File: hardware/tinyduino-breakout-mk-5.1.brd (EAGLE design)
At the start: 24 x 22 mm, 12 parts, among them J1 DF12-32-DP-NOTREALLYREV

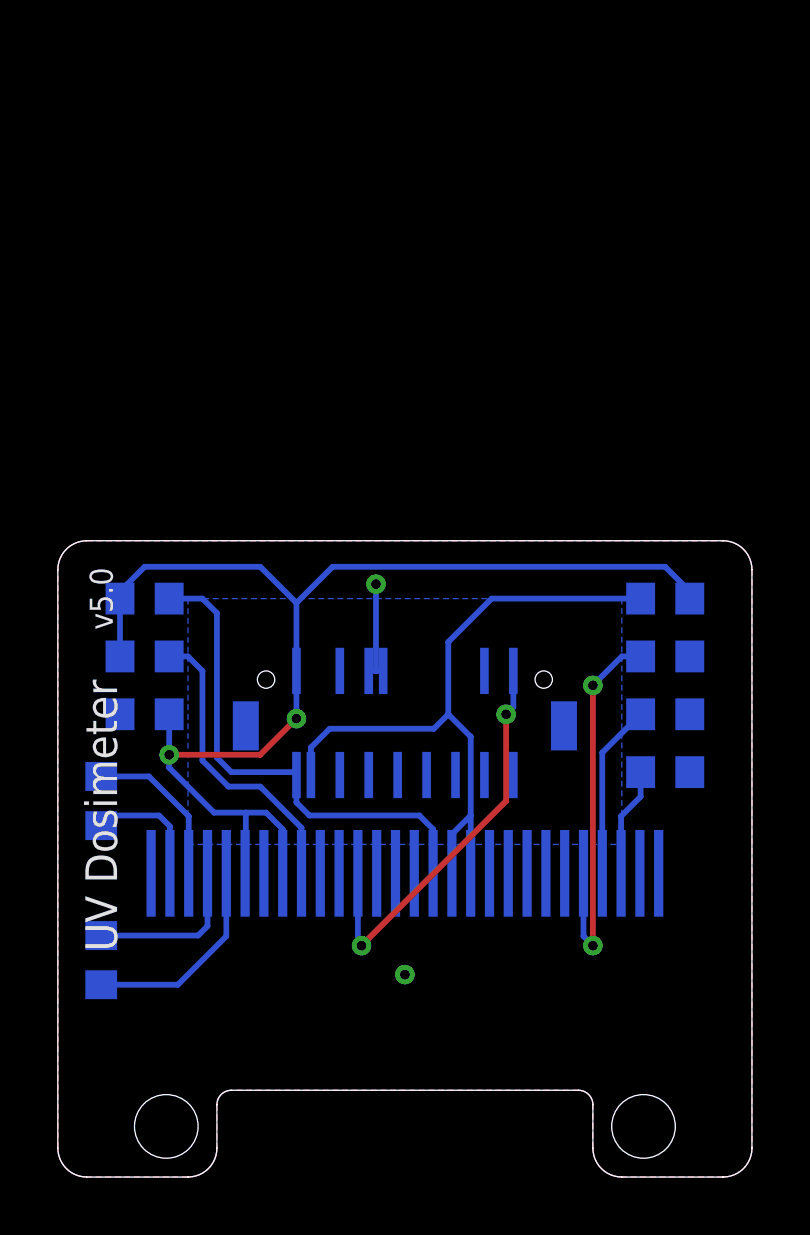
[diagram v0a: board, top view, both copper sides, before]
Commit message: breakouts for the tinyduino version
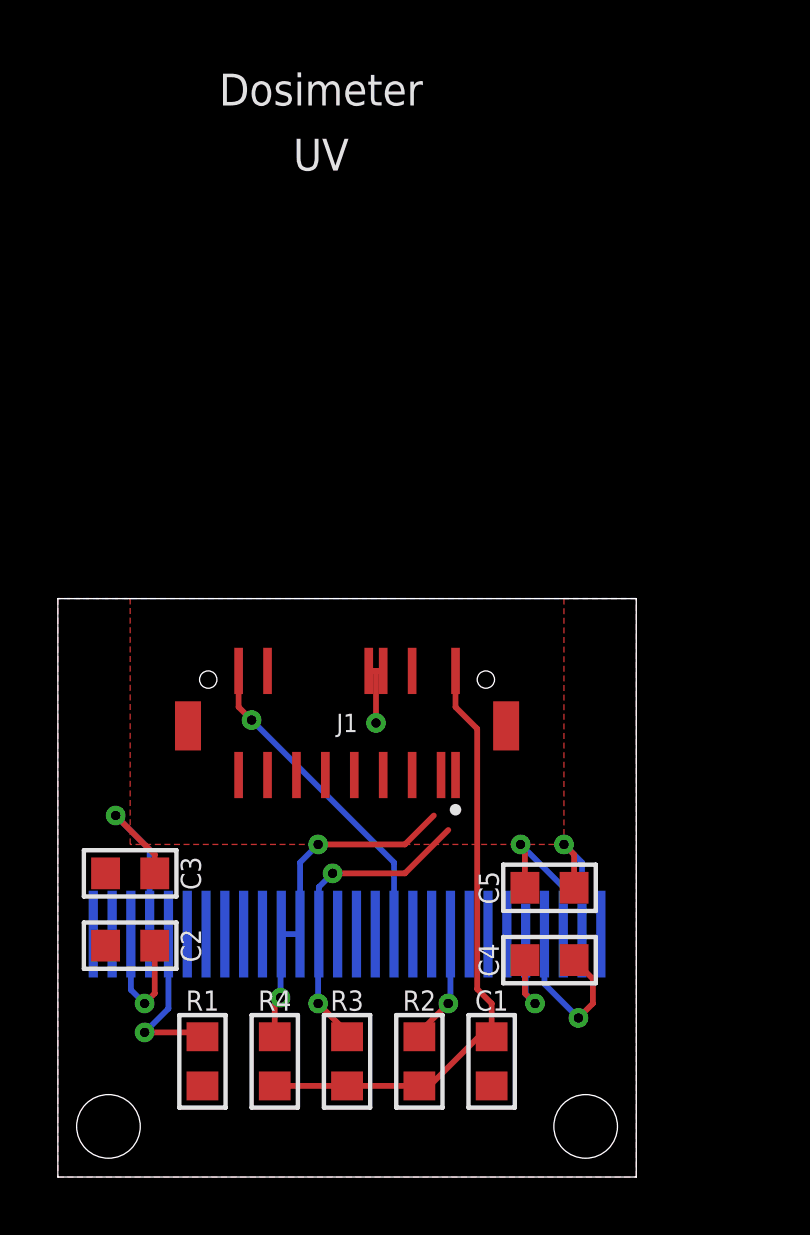
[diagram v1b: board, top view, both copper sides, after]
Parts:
- DISP1: value ER-OLED0.66-1FOLDED -> ER-OLED0.66-1FOLDED-SAME; device a_parts:ER-OLED0.66-1-FOLDED -> a_parts:ER-OLED0.66-1-FOLDED-SAME
- moved R1 21.3 mm to (5.00, 4.00), flipped to the top, turned to 90 degrees
- moved R4 20.9 mm to (7.50, 4.00), flipped to the top, turned to 270 degrees
- moved FRAME1 20.0 mm to (20.0, 0.00), flipped to the bottom
- moved C2 19.4 mm to (2.50, 8.00), flipped to the top
- moved C3 19.3 mm to (2.50, 10.5), flipped to the top
- moved R3 17.5 mm to (10.0, 4.00), flipped to the top, turned to 270 degrees
- moved C1 17.0 mm to (15.0, 4.00), flipped to the top, turned to 270 degrees
- moved R2 16.9 mm to (12.5, 4.00), flipped to the top, turned to 270 degrees
- moved C5 15.8 mm to (17.0, 10.0), flipped to the top, turned to 180 degrees
- moved C4 15.5 mm to (17.0, 7.50), flipped to the top, turned to 180 degrees
- moved DISP1 2.90 mm to (10.0, 8.40), flipped to the bottom
- moved J1 2.00 mm to (10.0, 15.7), flipped to the bottom
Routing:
- net VCC: track 43.1 -> 21.4 mm, vias 2 -> 0
- net SDA: track 24.0 -> 12.1 mm, vias 0 -> 2
- net N$3: track 13.7 -> 5.80 mm, vias 2 -> 1
- net SCL: track 17.4 -> 10.9 mm, vias 0 -> 2
- net N$9: track 10.4 -> 4.00 mm, vias 0 -> 1
- net N$5: track 7.19 -> 4.18 mm, vias 0 -> 1
- net DRST: track 14.2 -> 11.3 mm, vias 2 -> 1
- net GND: track 3.50 -> 2.30 mm, vias 2 -> 1
- net N$2: track 6.05 -> 7.15 mm, vias 0 -> 1
- net N$1: track 3.78 -> 4.74 mm, vias 0 -> 1
- net N$6: track 4.30 -> 5.00 mm, vias 0 -> 1
- net N$7: track 5.57 -> 5.27 mm, vias 0 -> 1
- net N$4: track 5.63 -> 5.86 mm, vias 0 -> 1
- removed copper zone on layer 16, net N$8
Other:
- board size 24 x 22 mm -> 20 x 20 mm
- board text added: "Dosimeter"
- board text added: "Tinyduino + Adafruit Si1145"
- board text added: "UV"
- board text added: "by schizobovine <sean@yak.net> CC-4.0-BY-SA"
- board text removed: "by sean@yak.net CC-4.0-BY-SA"
